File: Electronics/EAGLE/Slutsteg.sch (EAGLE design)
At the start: 152 parts, among them CN1 OSTYK33102030-2, CN2 OSTYK33102030-2, CN3 OSTYK33102030-2, IC1 SPX1117M3-L-3-3_TR, IC10 LM324D, IC11 L78M12ABDT-TR, IC3 ESP32-WROVER-IE-4MB, IC4 TM8211, IC6 TPA3244DDWR, IC7 TPA3251D2DDVR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

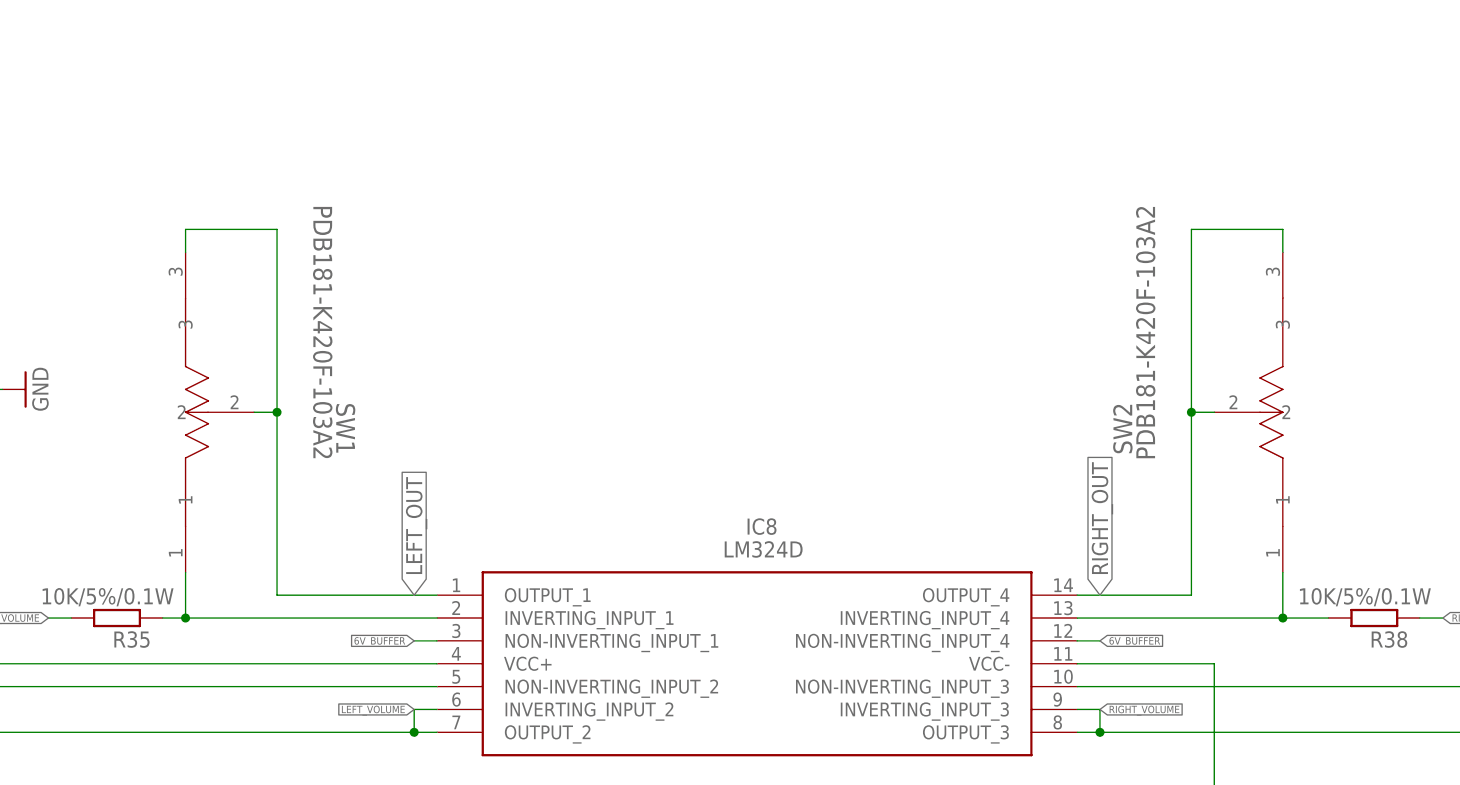
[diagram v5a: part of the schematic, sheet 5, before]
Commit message: Lagt till double-gang pot och petat lite i layouten
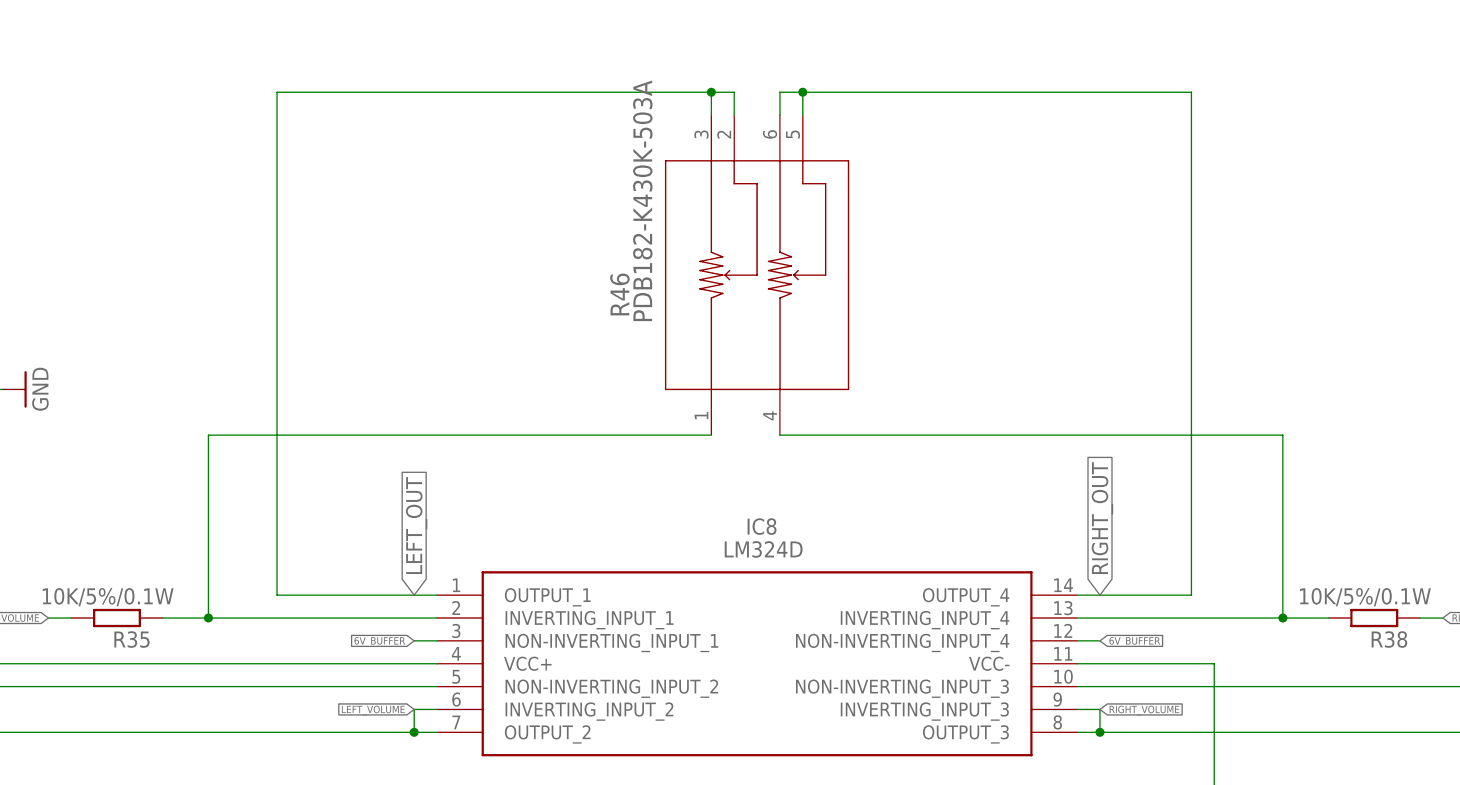
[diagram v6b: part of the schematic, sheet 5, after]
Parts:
- removed SW1, SW2: PDB181-K420F-103A2, PDB181-K420F-103A2:PDB181-K420F-103A2
- added R46: PDB182-K430K-503A, Pot-PDB18:PDB182-K430K-503A
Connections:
- net LEFT_OUT: now also R46.2, R46.3; no longer SW1.2, SW1.3
- net N$71: now also R46.1; no longer SW1.1
- net N$74: now also R46.4; no longer SW2.1
- net RIGHT_OUT: now also R46.5, R46.6; no longer SW2.2, SW2.3
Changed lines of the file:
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@@
 <part name="VDD10" library="supply1" library_urn="urn:adsk.eagle:library:371" deviceset="VDD" device=""/>
 <part name="GND24" library="supply1" library_urn="urn:adsk.eagle:library:371" deviceset="GND" device=""/>
-<part name="SW1" library="PDB181-K420F-103A2" deviceset="PDB181-K420F-103A2" device=""/>
 <part name="IC9" library="SamacSys_Parts" deviceset="LM324D" device=""/>
 <part name="R40" library="rcl" library_urn="urn:adsk.eagle:library:334" deviceset="R-EU_" device="R0603" package3d_urn="urn:adsk.eagle:package:23555/3" value="100K/5%/0.1W"/>
@@
 <part name="R41" library="rcl" library_urn="urn:adsk.eagle:library:334" deviceset="R-EU_" device="R0603" package3d_urn="urn:adsk.eagle:package:23555/3" value="10K/5%/0.1W"/>
 <part name="R38" library="rcl" library_urn="urn:adsk.eagle:library:334" deviceset="R-EU_" device="R0603" package3d_urn="urn:adsk.eagle:package:23555/3" value="10K/5%/0.1W"/>
-<part name="SW2" library="PDB181-K420F-103A2" deviceset="PDB181-K420F-103A2" device=""/>
 <part name="FRAME5" library="frames" library_urn="urn:adsk.eagle:library:229" deviceset="A3L-LOC" device=""/>
 <part name="C77" library="rcl" library_urn="urn:adsk.eagle:library:334" deviceset="C-EU" device="C0603" package3d_urn="urn:adsk.eagle:package:23616/2" value="100nF/50V"/>
@@
 <part name="R45" library="rcl" library_urn="urn:adsk.eagle:library:334" deviceset="R-EU_" device="R0603" package3d_urn="urn:adsk.eagle:package:23555/3" value="10K/5%/0.1W"/>
 <part name="CN3" library="OSTYK33108030" deviceset="OSTYK33102030-2" device="" override_package3d_urn="urn:adsk.eagle:package:27162182/2" override_package_urn="urn:adsk.eagle:footprint:27162183/1"/>
+<part name="R46" library="Pot-PDB18" deviceset="PDB182-K430K-503A" device=""/>
 </parts>
 <sheets>
@@
 <attribute name="VALUE" x="259.08" y="38.1" size="1.778" layer="96" rot="MR0"/>
 </instance>
-<instance part="SW1" gate="A" x="129.54" y="193.04" smashed="yes" rot="MR90">
-<attribute name="NAME" x="146.2786" y="208.6356" size="2.0828" layer="95" ratio="6" rot="SMR90"/>
-<attribute name="VALUE" x="143.7386" y="208.0006" size="2.0828" layer="96" ratio="6" rot="SMR90"/>
-</instance>
 <instance part="IC9" gate="G$1" x="172.72" y="81.28" smashed="yes">
 <attribute name="NAME" x="207.01" y="88.9" size="1.778" layer="95" align="center-left"/>
@@
 <attribute name="VALUE" x="267.97" y="193.802" size="1.778" layer="96" rot="R180"/>
 </instance>
-<instance part="SW2" gate="A" x="251.46" y="193.04" smashed="yes" rot="R90">
-<attribute name="NAME" x="234.7214" y="208.6356" size="2.0828" layer="95" ratio="6" rot="SR90"/>
-<attribute name="VALUE" x="237.2614" y="208.0006" size="2.0828" layer="96" ratio="6" rot="SR90"/>
-</instance>
 <instance part="FRAME5" gate="G$1" x="0" y="0" smashed="yes">
 <attribute name="DRAWING_NAME" x="344.17" y="15.24" size="2.54" layer="94"/>
@@
 <attribute name="VALUE" x="136.144" y="46.101" size="1.778" layer="96"/>
 </instance>
+<instance part="R46" gate="A" x="187.96" y="208.28" smashed="yes" rot="R90">
+<attribute name="NAME" x="178.8414" y="223.8756" size="2.0828" layer="95" ratio="6" rot="SR90"/>
+<attribute name="VALUE" x="181.3814" y="223.2406" size="2.0828" layer="96" ratio="6" rot="SR90"/>
+</instance>
 </instances>
 <busses>
@@
 <pinref part="IC8" gate="G$1" pin="INVERTING_INPUT_1"/>
 <pinref part="R35" gate="G$1" pin="1"/>
-<wire x1="157.48" y1="190.5" x2="129.54" y2="190.5" width="0.1524" layer="91"/>
-<pinref part="SW1" gate="A" pin="1"/>
-<wire x1="129.54" y1="190.5" x2="127" y2="190.5" width="0.1524" layer="91"/>
-<wire x1="129.54" y1="195.58" x2="129.54" y2="190.5" width="0.1524" layer="91"/>
-<junction x="129.54" y="190.5"/>
+<wire x1="157.48" y1="190.5" x2="132.08" y2="190.5" width="0.1524" layer="91"/>
+<pinref part="R46" gate="A" pin="1"/>
+<wire x1="132.08" y1="190.5" x2="127" y2="190.5" width="0.1524" layer="91"/>
+<wire x1="132.08" y1="190.5" x2="132.08" y2="210.82" width="0.1524" layer="91"/>
+<wire x1="132.08" y1="210.82" x2="187.96" y2="210.82" width="0.1524" layer="91"/>
+<junction x="132.08" y="190.5"/>
 </segment>
 </net>
 <net name="LEFT_OUT" class="0">
 <segment>
-<pinref part="SW1" gate="A" pin="3"/>
-<wire x1="129.54" y1="231.14" x2="129.54" y2="233.68" width="0.1524" layer="91"/>
-<wire x1="129.54" y1="233.68" x2="139.7" y2="233.68" width="0.1524" layer="91"/>
-<wire x1="139.7" y1="233.68" x2="139.7" y2="213.36" width="0.1524" layer="91"/>
-<pinref part="SW1" gate="A" pin="2"/>
-<wire x1="139.7" y1="213.36" x2="137.16" y2="213.36" width="0.1524" layer="91"/>
 <pinref part="IC8" gate="G$1" pin="OUTPUT_1"/>
-<wire x1="139.7" y1="213.36" x2="139.7" y2="193.04" width="0.1524" layer="91"/>
 <wire x1="139.7" y1="193.04" x2="157.48" y2="193.04" width="0.1524" layer="91"/>
-<junction x="139.7" y="213.36"/>
 <label x="154.94" y="193.04" size="1.778" layer="95" rot="R90" xref="yes"/>
+<pinref part="R46" gate="A" pin="2"/>
+<wire x1="190.5" y1="246.38" x2="190.5" y2="248.92" width="0.1524" layer="91"/>
+<wire x1="190.5" y1="248.92" x2="187.96" y2="248.92" width="0.1524" layer="91"/>
+<pinref part="R46" gate="A" pin="3"/>
+<wire x1="187.96" y1="248.92" x2="187.96" y2="246.38" width="0.1524" layer="91"/>
+<wire x1="139.7" y1="193.04" x2="139.7" y2="248.92" width="0.1524" layer="91"/>
+<wire x1="139.7" y1="248.92" x2="187.96" y2="248.92" width="0.1524" layer="91"/>
+<junction x="187.96" y="248.92"/>
 </segment>
 </net>
@@
 <pinref part="R38" gate="G$1" pin="2"/>
 <wire x1="228.6" y1="190.5" x2="251.46" y2="190.5" width="0.1524" layer="91"/>
-<pinref part="SW2" gate="A" pin="1"/>
 <wire x1="251.46" y1="190.5" x2="256.54" y2="190.5" width="0.1524" layer="91"/>
-<wire x1="251.46" y1="195.58" x2="251.46" y2="190.5" width="0.1524" layer="91"/>
 <junction x="251.46" y="190.5"/>
+<wire x1="251.46" y1="190.5" x2="251.46" y2="210.82" width="0.1524" layer="91"/>
+<pinref part="R46" gate="A" pin="4"/>
+<wire x1="251.46" y1="210.82" x2="195.58" y2="210.82" width="0.1524" layer="91"/>
 </segment>
 </net>
 <net name="RIGHT_OUT" class="0">
 <segment>
-<pinref part="SW2" gate="A" pin="3"/>
-<wire x1="251.46" y1="231.14" x2="251.46" y2="233.68" width="0.1524" layer="91"/>
-<wire x1="251.46" y1="233.68" x2="241.3" y2="233.68" width="0.1524" layer="91"/>
-<wire x1="241.3" y1="233.68" x2="241.3" y2="213.36" width="0.1524" layer="91"/>
-<pinref part="SW2" gate="A" pin="2"/>
-<wire x1="241.3" y1="213.36" x2="243.84" y2="213.36" width="0.1524" layer="91"/>
 <pinref part="IC8" gate="G$1" pin="OUTPUT_4"/>
 <wire x1="228.6" y1="193.04" x2="241.3" y2="193.04" width="0.1524" layer="91"/>
-<wire x1="241.3" y1="193.04" x2="241.3" y2="213.36" width="0.1524" layer="91"/>
-<junction x="241.3" y="213.36"/>
+<wire x1="241.3" y1="193.04" x2="241.3" y2="248.92" width="0.1524" layer="91"/>
 <label x="231.14" y="193.04" size="1.778" layer="95" rot="R90" xref="yes"/>
+<pinref part="R46" gate="A" pin="6"/>
+<wire x1="195.58" y1="246.38" x2="195.58" y2="248.92" width="0.1524" layer="91"/>
+<pinref part="R46" gate="A" pin="5"/>
+<wire x1="195.58" y1="248.92" x2="198.12" y2="248.92" width="0.1524" layer="91"/>
+<wire x1="198.12" y1="248.92" x2="198.12" y2="246.38" width="0.1524" layer="91"/>
+<wire x1="241.3" y1="248.92" x2="198.12" y2="248.92" width="0.1524" layer="91"/>
+<junction x="198.12" y="248.92"/>
 </segment>
 </net>

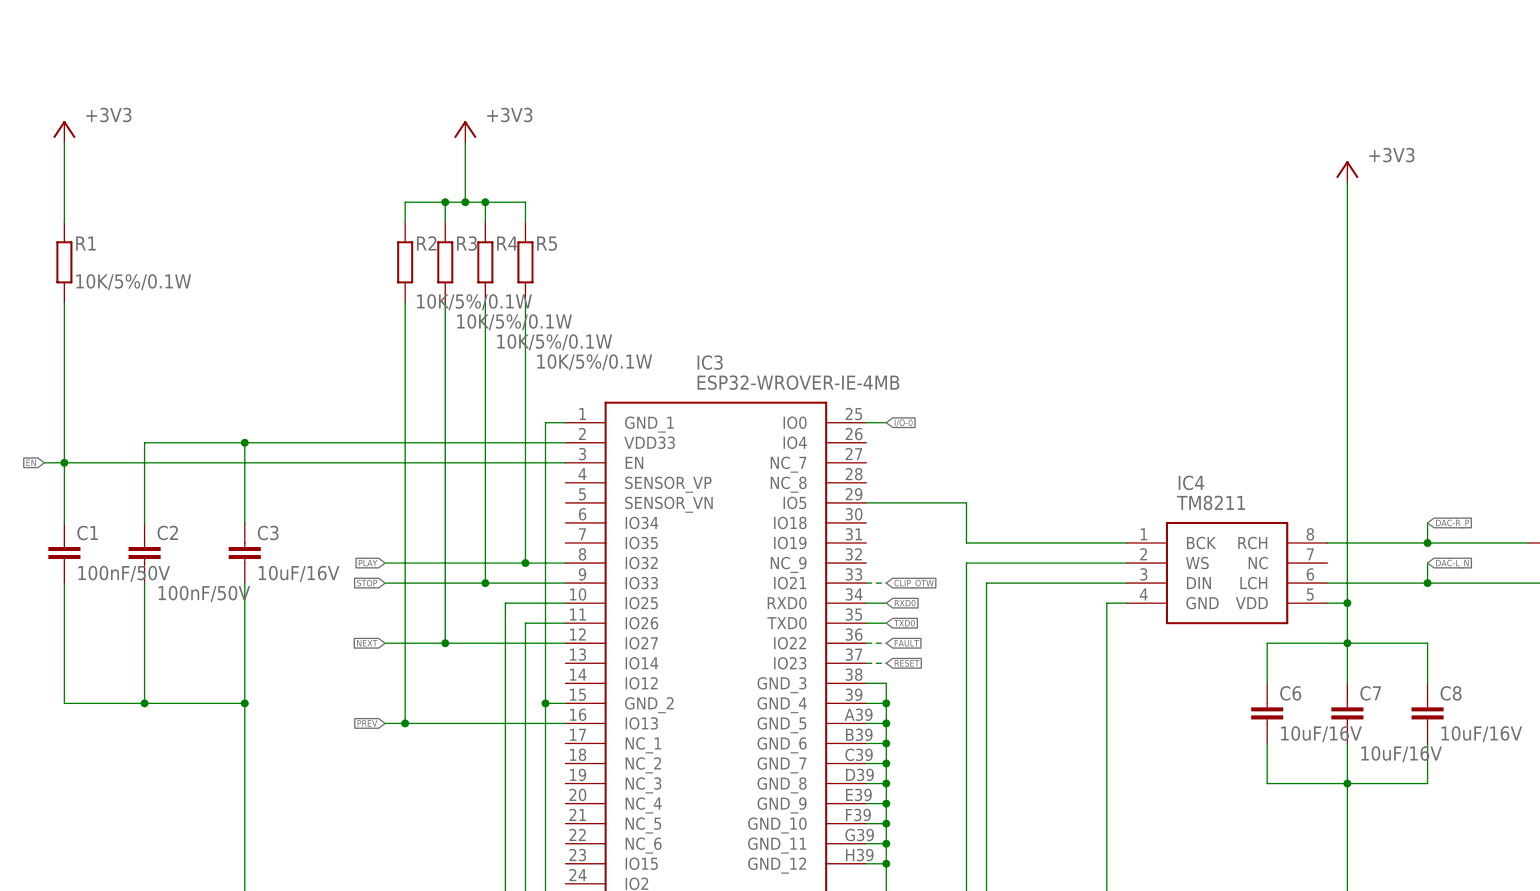
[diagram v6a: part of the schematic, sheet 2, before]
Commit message: Continued with layout and fixed minor issues with the schematic.
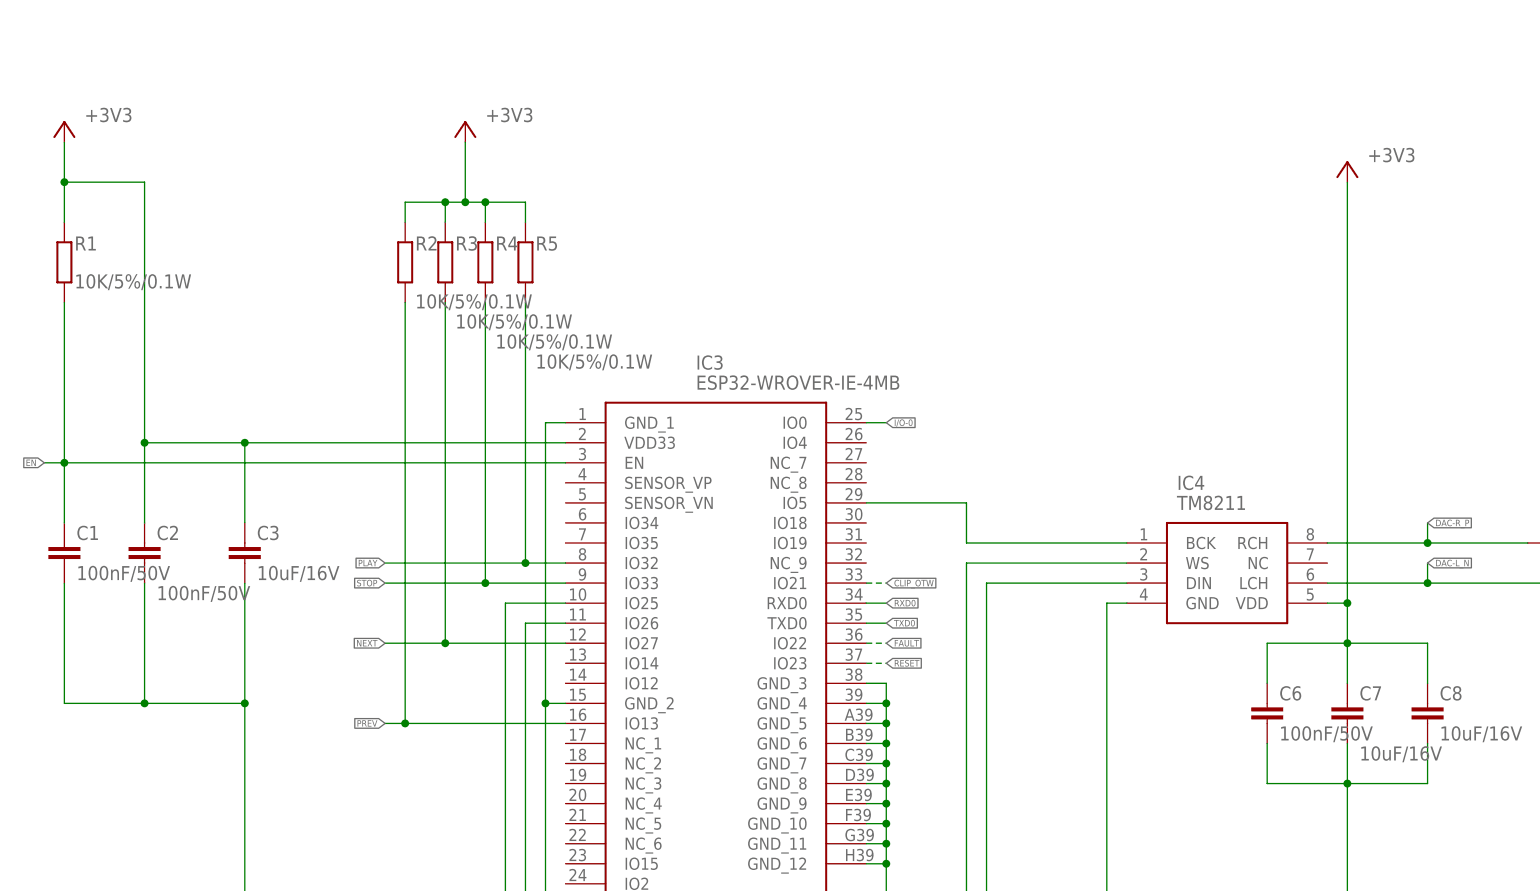
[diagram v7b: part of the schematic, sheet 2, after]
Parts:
- C6: value 10uF/16V -> 100nF/50V; device rcl:C-EUC0805 -> rcl:C-EUC0603
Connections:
- removed net N$75: C2.1, C3.1, IC3.VDD33
- net +3V3: now also C2.1, C3.1, IC3.VDD33
